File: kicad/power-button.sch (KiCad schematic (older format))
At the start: 13 parts, among them J1 12V, Q1 D4184A, U1 LM2596, U2 ATTINY13-20SSU

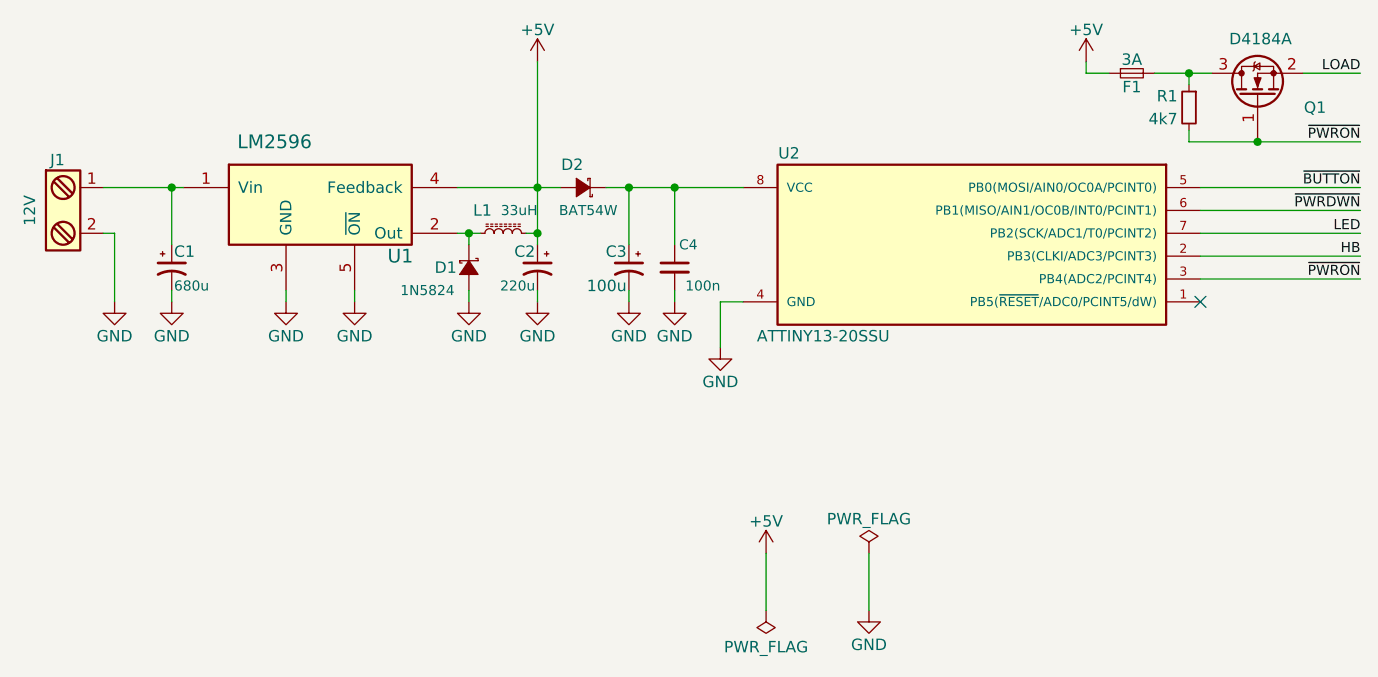
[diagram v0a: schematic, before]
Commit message: Set footprint for all components.
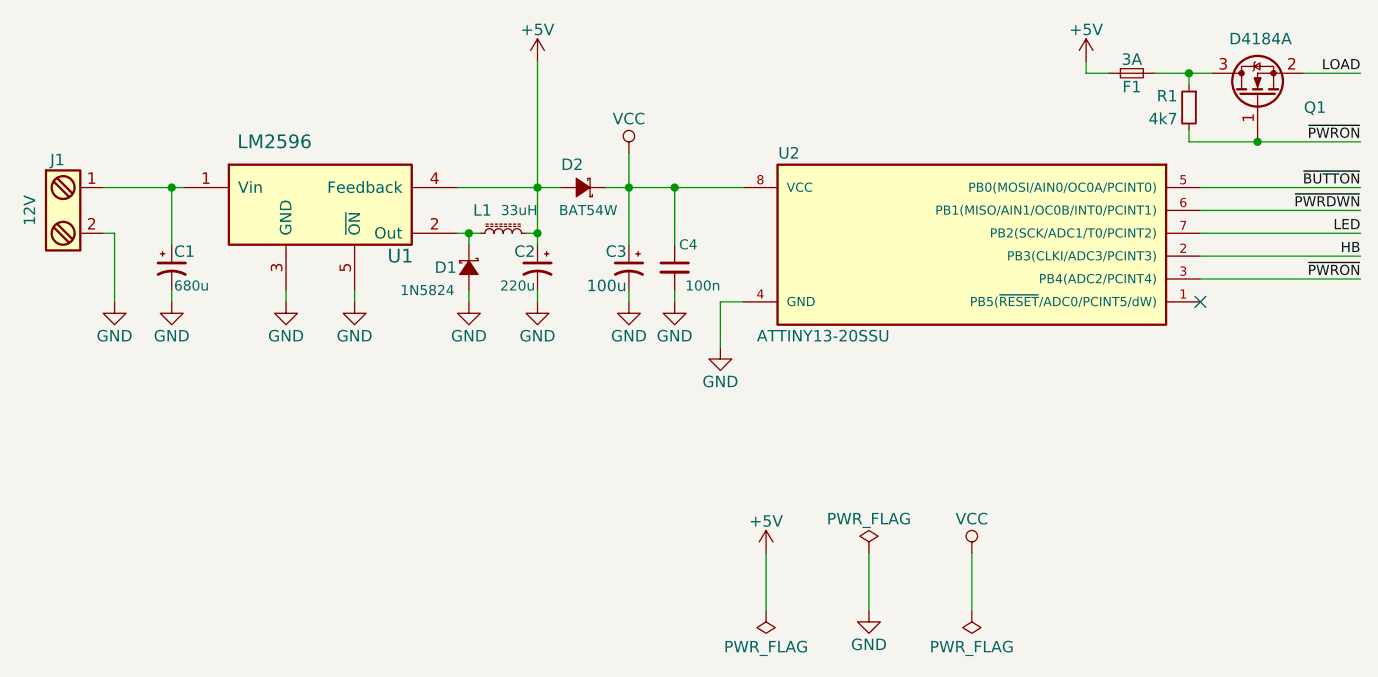
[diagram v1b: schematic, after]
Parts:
- C1: footprint (none) -> Capacitors_THT:CP_Radial_D10.0mm_P5.00mm_P7.50mm
- C2: footprint (none) -> Capacitors_THT:CP_Radial_D8.0mm_P3.50mm
- C3: footprint (none) -> Capacitors_THT:CP_Radial_D7.5mm_P2.50mm
- D1: footprint (none) -> Diodes_THT:D_DO-201AD_P12.70mm_Horizontal
- D2: footprint (none) -> Diodes_SMD:D_1206
- J1: footprint (none) -> Connectors_Terminal_Blocks:TerminalBlock_4UCON_19963_02x3.5mm_Straight
- L1: footprint (none) -> Choke_Toroid_ThroughHole:Choke_Toroid_6,5x13mm_Vertical
- R1: footprint (none) -> Resistors_SMD:R_1206_HandSoldering
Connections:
- net VCC: now reaches C3.1, C4.1, D2.1 (K), U2.8 (VCC)
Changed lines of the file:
@@
 F 0 "C3" H 5610 3970 50  0000 L CNN
 F 1 "100u" H 5610 3820 50  0000 L CNN
-F 2 "" H 5600 3900 50  0001 C CNN
+F 2 "Capacitors_THT:CP_Radial_D7.5mm_P2.50mm" H 5600 3900 50  0001 C CNN
 F 3 "" H 5600 3900 50  0001 C CNN
 	1    5600 3900
@@
 F 0 "L1" V 5150 3800 50  0000 L CNN
 F 1 "33uH" V 5150 3600 44  0000 L CNN
-F 2 "" H 5050 3750 50  0001 C CNN
+F 2 "Choke_Toroid_ThroughHole:Choke_Toroid_6,5x13mm_Vertical" H 5050 3750 50  0001 C CNN
 F 3 "" H 5050 3750 50  0001 C CNN
 	1    5050 3750
@@
 F 0 "D1" V 4900 3750 50  0000 L CNN
 F 1 "1N5824" V 5000 3600 44  0000 L CNN
-F 2 "" V 4900 3900 50  0001 C CNN
+F 2 "Diodes_THT:D_DO-201AD_P12.70mm_Horizontal" V 4900 3900 50  0001 C CNN
 F 3 "" V 4900 3900 50  0001 C CNN
 	1    4900 3900
@@
 F 0 "C2" H 5210 3970 50  0000 L CNN
 F 1 "220u" H 5210 3820 44  0000 L CNN
-F 2 "" H 5200 3900 50  0001 C CNN
+F 2 "Capacitors_THT:CP_Radial_D8.0mm_P3.50mm" H 5200 3900 50  0001 C CNN
 F 3 "" H 5200 3900 50  0001 C CNN
 	1    5200 3900
@@
 F 0 "C1" H 3610 3970 50  0000 L CNN
 F 1 "680u" H 3610 3820 44  0000 L CNN
-F 2 "" H 3600 3900 50  0001 C CNN
+F 2 "Capacitors_THT:CP_Radial_D10.0mm_P5.00mm_P7.50mm" H 3600 3900 50  0001 C CNN
 F 3 "" H 3600 3900 50  0001 C CNN
 	1    3600 3900
@@
 F 0 "J1" H 3100 3900 50  0000 C TNN
 F 1 "12V" V 2950 3650 50  0000 C TNN
-F 2 "" H 3100 3425 50  0001 C CNN
+F 2 "Connectors_Terminal_Blocks:TerminalBlock_4UCON_19963_02x3.5mm_Straight" H 3100 3425 50  0001 C CNN
 F 3 "" H 3075 3650 50  0001 C CNN
 	1    3100 3650
@@
 	4850 3750 4950 3750
 Wire Wire Line
-	5600 3550 5600 3800
+	5600 3400 5600 3800
 $Comp
 L 2N7002 Q1
@@
 F 0 "D2" H 5400 3450 50  0000 L CNN
 F 1 "BAT54W" H 5250 3650 44  0000 L CNN
-F 2 "" V 5400 3550 50  0001 C CNN
+F 2 "Diodes_SMD:D_1206" V 5400 3550 50  0001 C CNN
 F 3 "" V 5400 3550 50  0001 C CNN
 	1    5400 3550
@@
 F 0 "R1" H 8100 3250 50  0000 L CNN
 F 1 "4k7" H 8100 3150 50  0000 L CNN
-F 2 "" H 8050 3200 50  0001 C CNN
+F 2 "Resistors_SMD:R_1206_HandSoldering" H 8050 3200 50  0001 C CNN
 F 3 "" H 8050 3200 50  0001 C CNN
 	1    8050 3200
@@
 Wire Wire Line
 	8100 3650 8800 3650
+$Comp
+L VCC #PWR016
+U 1 1 5A79EF6A
+P 5600 3400
+F 0 "#PWR016" H 5600 3250 50  0001 C CNN
+F 1 "VCC" H 5600 3550 50  0000 C CNN
+F 2 "" H 5600 3400 50  0001 C CNN
+F 3 "" H 5600 3400 50  0001 C CNN
+	1    5600 3400
+	1    0    0    -1
+$EndComp
+$Comp
+L VCC #PWR017
+U 1 1 5A79F05F
+P 7100 5150
+F 0 "#PWR017" H 7100 5000 50  0001 C CNN
+F 1 "VCC" H 7100 5300 50  0000 C CNN
+F 2 "" H 7100 5150 50  0001 C CNN
+F 3 "" H 7100 5150 50  0001 C CNN
+	1    7100 5150
+	1    0    0    -1
+$EndComp
+$Comp
+L PWR_FLAG #FLG018
+U 1 1 5A79F091
+P 7100 5400
+F 0 "#FLG018" H 7100 5475 50  0001 C CNN
+F 1 "PWR_FLAG" H 7100 5560 50  0000 C CNN
+F 2 "" H 7100 5400 50  0001 C CNN
+F 3 "" H 7100 5400 50  0001 C CNN
+	1    7100 5400
+	-1   0    0    1
+$EndComp
+Wire Wire Line
+	7100 5400 7100 5150
 $EndSCHEMATC

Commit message: Change pinout according to new design
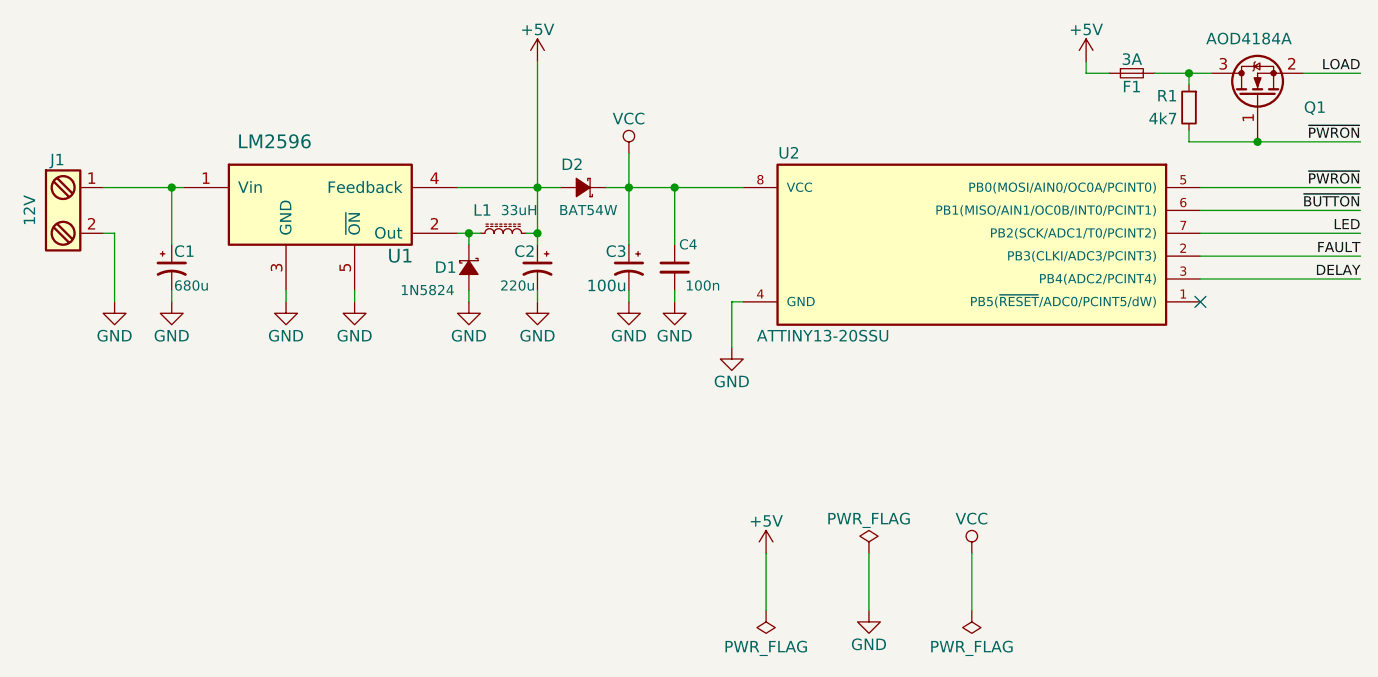
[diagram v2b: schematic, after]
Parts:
- Q1: value D4184A -> AOD4184A
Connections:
- net ~PWRDWN is gone; now on net ~BUTTON: U2.6 (PB1(MISO/AIN1/OC0B/INT0/PCINT1))
- net ~BUTTON: no longer U2.5 (PB0(MOSI/AIN0/OC0A/PCINT0))
- net ~PWRON: now also U2.5 (PB0(MOSI/AIN0/OC0A/PCINT0)); no longer U2.3 (PB4(ADC2/PCINT4))
- net HB renamed FAULT
- new net DELAY: U2.3 (PB4(ADC2/PCINT4))
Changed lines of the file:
@@
 $EndComp
 Text Label 8800 3850 2    44   ~ 0
-HB
-Text Label 8800 3950 2    44   ~ 0
+FAULT
+Text Label 8800 3550 2    44   ~ 0
 ~PWRON
 $Comp
@@
 	-1   0    0    -1
 $EndComp
-Wire Wire Line
-	6000 4250 6000 4050
-Wire Wire Line
-	6000 4050 6100 4050
 $Comp
 L GND #PWR06
 U 1 1 5A367BD2
-P 6000 4250
-F 0 "#PWR06" H 6000 4000 50  0001 C CNN
-F 1 "GND" H 6000 4100 50  0000 C CNN
-F 2 "" H 6000 4250 50  0000 C CNN
-F 3 "" H 6000 4250 50  0000 C CNN
-	1    6000 4250
+P 6050 4250
+F 0 "#PWR06" H 6050 4000 50  0001 C CNN
+F 1 "GND" H 6050 4100 50  0000 C CNN
+F 2 "" H 6050 4250 50  0000 C CNN
+F 3 "" H 6050 4250 50  0000 C CNN
+	1    6050 4250
 	1    0    0    -1
 $EndComp
@@
 P 8350 3150
 F 0 "Q1" V 8300 2850 50  0000 L CNN
-F 1 "D4184A" V 8600 3000 50  0000 L CNN
+F 1 "AOD4184A" V 8600 3000 50  0000 L CNN
 F 2 "TO_SOT_Packages_SMD:SOT-23" H 8550 3075 50  0001 L CIN
 F 3 "" H 8350 3150 50  0001 L CNN
@@
 Wire Wire Line
 	5600 4050 5600 4000
-Text Label 8800 3550 2    44   ~ 0
+Text Label 8800 3650 2    44   ~ 0
 ~BUTTON
 Wire Wire Line
@@
 Wire Wire Line
 	8100 3550 8800 3550
-Text Label 8800 3650 2    44   ~ 0
-~PWRDWN
 Wire Wire Line
 	8100 3650 8800 3650
@@
 Wire Wire Line
 	7100 5400 7100 5150
+Wire Wire Line
+	6050 4250 6050 4050
+Wire Wire Line
+	6050 4050 6100 4050
+Text Label 8800 3950 2    44   ~ 0
+DELAY
 $EndSCHEMATC
